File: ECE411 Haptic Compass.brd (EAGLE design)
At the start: 63.5 x 63.2 mm, 40 parts, among them IC1 SN74LVC1G14DBVR, Q1 PBHV8115TLHR, Q2 PBHV8115TLHR, Q3 PBHV8115TLHR, Q4 PBHV8115TLHR, U1 328P, Y1 ECS-160-8-30Q-VY-TR

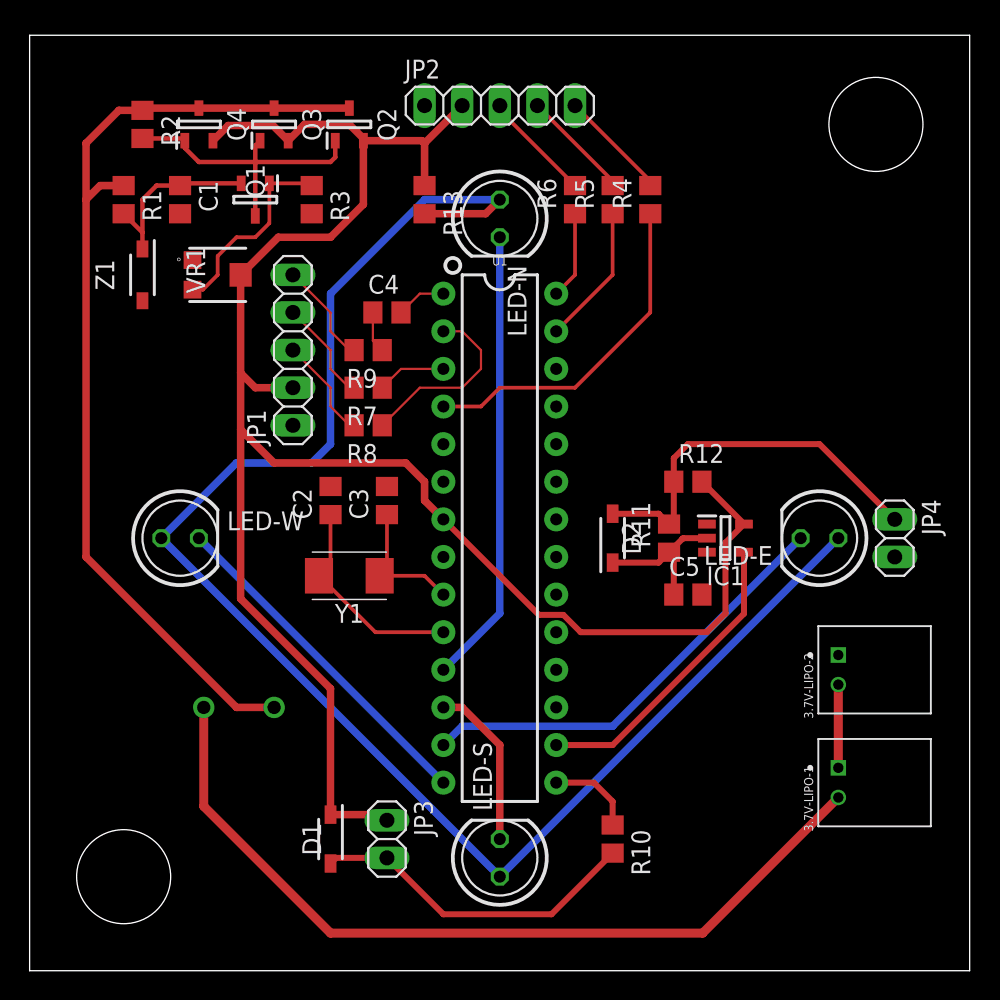
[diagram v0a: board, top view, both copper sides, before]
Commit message: Layout Finish - Ground Plane Added
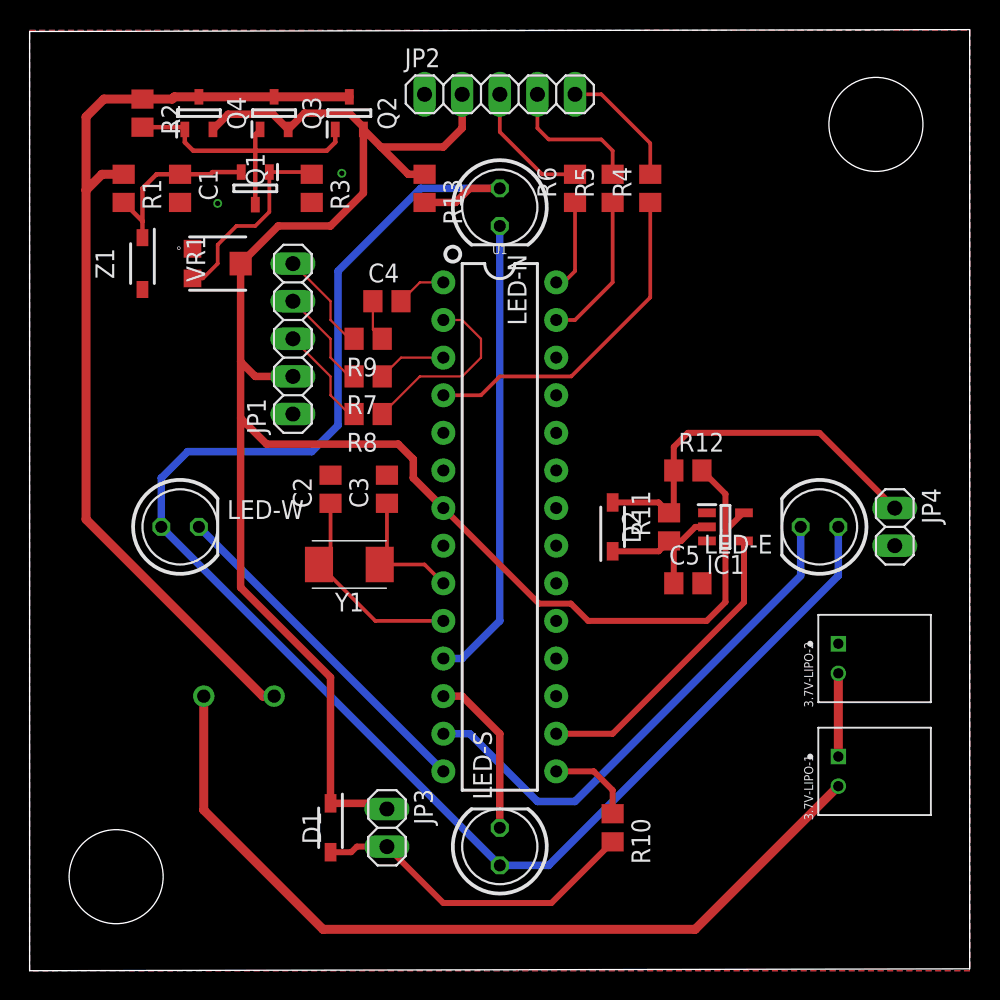
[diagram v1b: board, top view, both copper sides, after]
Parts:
- moved 3.7V-LIPO-1 0.76 mm to (54.6, 13.5)
- moved 3.7V-LIPO-2 0.76 mm to (54.6, 21.1)
- moved C1 0.76 mm to (10.2, 52.8)
- moved C2 0.76 mm to (20.3, 32.5)
- moved C3 0.76 mm to (24.1, 32.5)
- moved C4 0.76 mm to (24.1, 45.2)
- moved C5 0.76 mm to (44.5, 26.2)
- moved D2 0.76 mm to (39.4, 30.0)
- moved IC1 0.76 mm to (47.0, 30.0)
- moved JP1 0.76 mm to (17.8, 42.7)
- moved JP2 0.76 mm to (31.8, 59.2)
- moved JP4 0.76 mm to (58.4, 30.0)
- moved LED-E 0.76 mm to (53.3, 30.0)
- moved LED-N 0.76 mm to (31.8, 51.6)
- moved LED-W 0.76 mm to (10.2, 30.0)
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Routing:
- net LED-EAST: track 29.9 -> 35.6 mm
- net VCC: track 142.3 -> 138.1 mm
- net LED-RAIL: track 108.4 -> 112.4 mm
- net SDA-PORT: track 7.50 -> 9.59 mm
- net SCL-PORT: track 7.50 -> 8.80 mm
- net DRDY-PORT: track 7.50 -> 8.55 mm
- net +V-SUPPLY: track 56.9 -> 57.9 mm
- net SDA: track 9.52 -> 10.3 mm
- net LED-NORTH: track 30.8 -> 31.5 mm
- added copper zone on layer 1, net GND
- added copper zone on layer 16, net GND
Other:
- board size 63.5 x 63.2 mm -> 63.5 x 63.6 mm

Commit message: Placement of switch on top
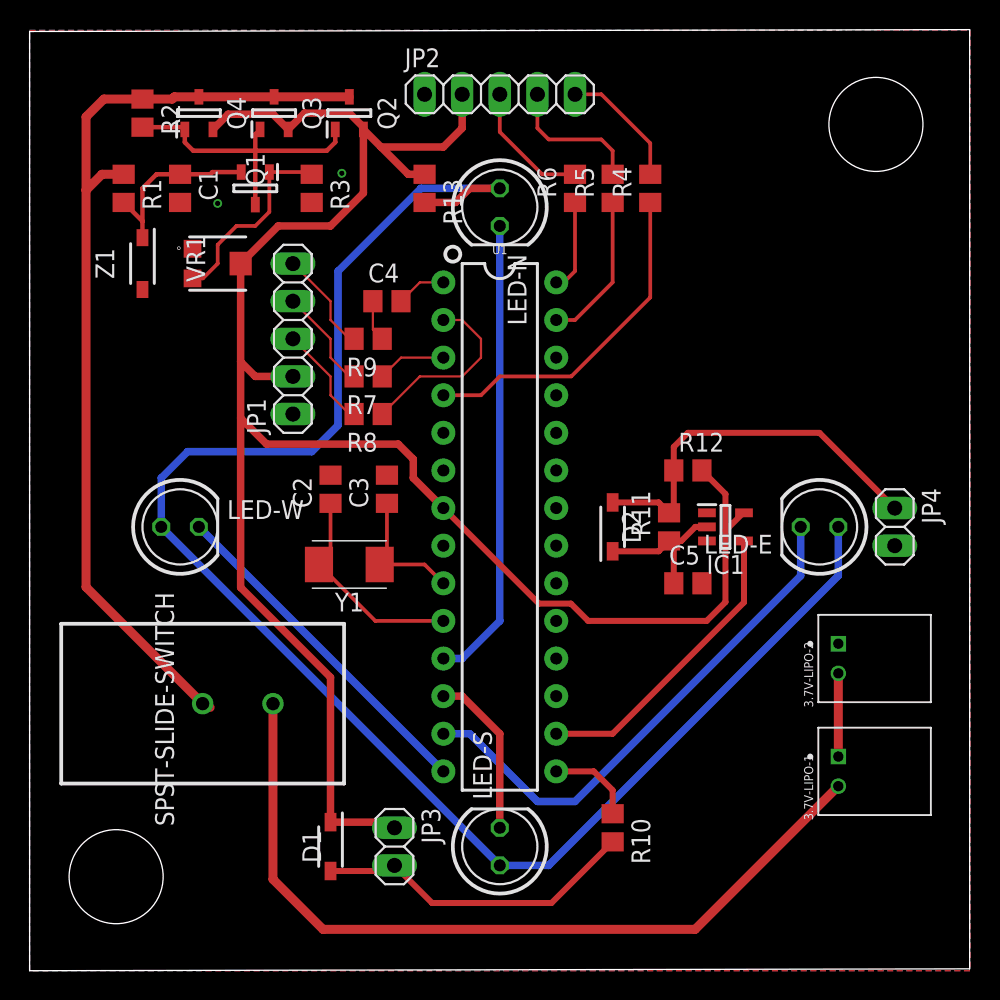
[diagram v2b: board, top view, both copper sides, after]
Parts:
- moved SPST-SLIDE-SWITCH 4.85 mm to (11.7, 18.0), flipped to the top
- moved JP3 1.37 mm to (24.6, 8.38)
- moved D1 1.27 mm to (20.3, 8.38)
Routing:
- net +V-SUPPLY: track 57.9 -> 55.4 mm
- net VCC: track 138.1 -> 139.9 mm
- net BJT-C: track 66.1 -> 64.8 mm
- net JP3-NEG: track 22.5 -> 22.0 mm

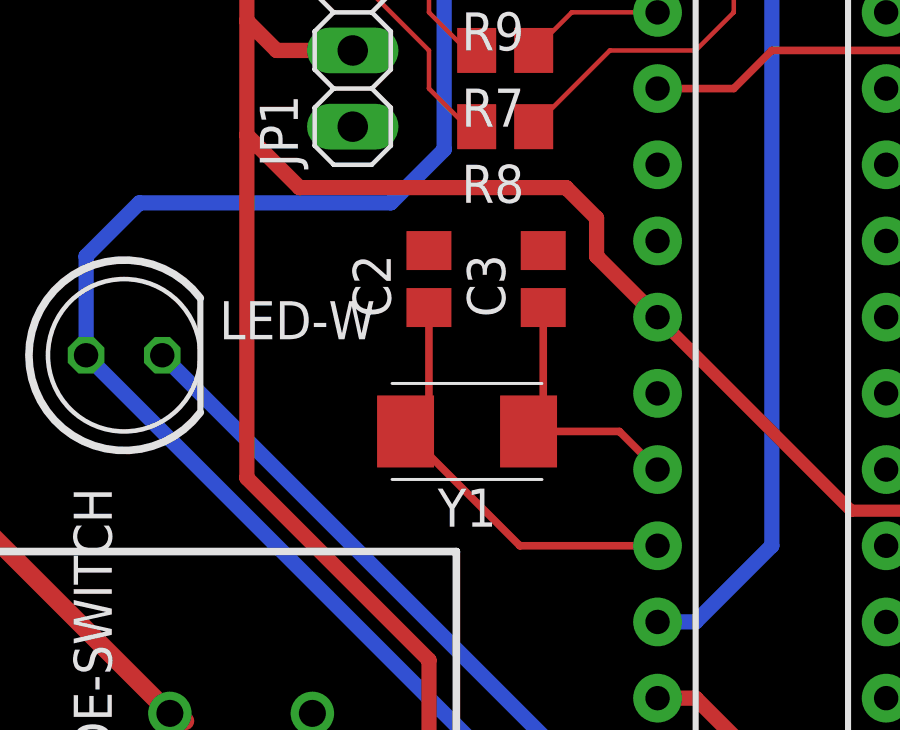
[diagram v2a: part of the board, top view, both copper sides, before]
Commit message: Included 1uF Capacitor next to Vcc for the uPC
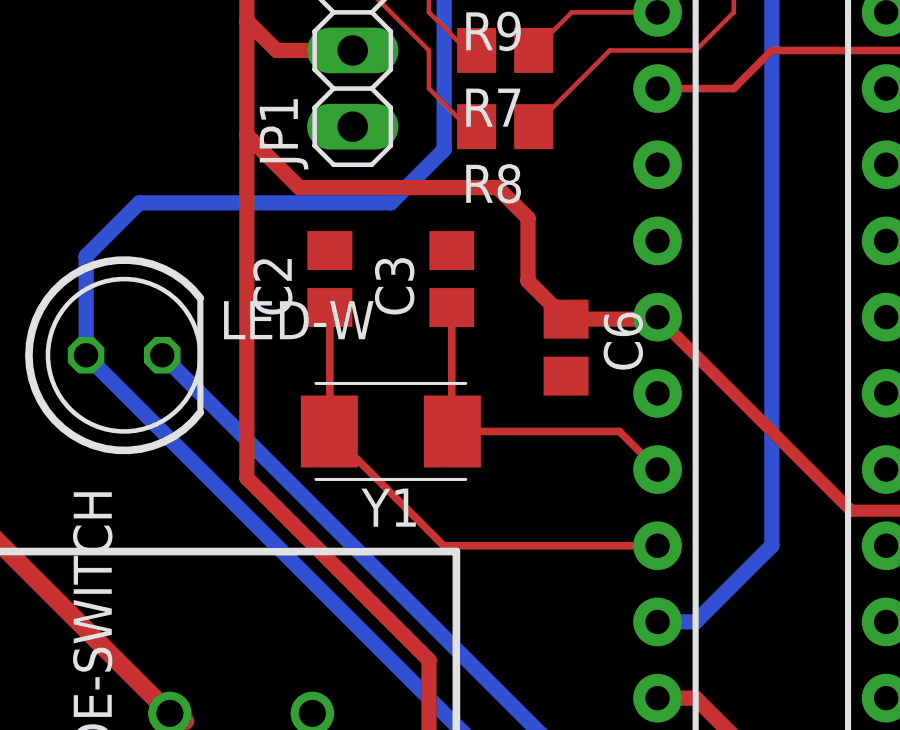
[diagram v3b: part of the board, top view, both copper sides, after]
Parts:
- added C6: 1uF, rcl:C0805
- moved C2 3.30 mm to (17.0, 32.5)
- moved C3 3.05 mm to (21.1, 32.5)
- moved Y1 2.54 mm to (19.1, 27.4)
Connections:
- net GND: now also C6.2
- net VCC: now also C6.1
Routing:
- net N$7: track 9.16 -> 11.5 mm
- net N$5: track 14.4 -> 16.7 mm
- net VCC: track 139.9 -> 140.4 mm
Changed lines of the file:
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@@
 <attribute name="VALUE" x="7.62" y="54.102" size="1.27" layer="27" rot="R270"/>
 </element>
-<element name="C2" library="rcl" library_urn="urn:adsk.eagle:library:334" package="C0805" package3d_urn="urn:adsk.eagle:package:23617/2" value="22pF" x="20.32" y="32.512" smashed="yes" rot="R90">
-<attribute name="NAME" x="19.05" y="31.242" size="1.27" layer="25" rot="R90"/>
-<attribute name="POPULARITY" value="63" x="60.96" y="82.042" size="1.778" layer="27" rot="R90" display="off"/>
-<attribute name="SPICEPREFIX" value="C" x="60.96" y="82.042" size="1.778" layer="27" rot="R90" display="off"/>
-<attribute name="VALUE" x="22.86" y="31.242" size="1.27" layer="27" rot="R90"/>
-</element>
-<element name="C3" library="rcl" library_urn="urn:adsk.eagle:library:334" package="C0805" package3d_urn="urn:adsk.eagle:package:23617/2" value="22pF" x="24.13" y="32.512" smashed="yes" rot="R90">
-<attribute name="NAME" x="22.86" y="31.242" size="1.27" layer="25" rot="R90"/>
-<attribute name="POPULARITY" value="63" x="64.77" y="88.392" size="1.778" layer="27" rot="R90" display="off"/>
-<attribute name="SPICEPREFIX" value="C" x="64.77" y="88.392" size="1.778" layer="27" rot="R90" display="off"/>
-<attribute name="VALUE" x="26.67" y="31.242" size="1.27" layer="27" rot="R90"/>
+<element name="C2" library="rcl" library_urn="urn:adsk.eagle:library:334" package="C0805" package3d_urn="urn:adsk.eagle:package:23617/2" value="22pF" x="17.018" y="32.512" smashed="yes" rot="R90">
+<attribute name="NAME" x="15.748" y="31.242" size="1.27" layer="25" rot="R90"/>
+<attribute name="POPULARITY" value="63" x="57.658" y="82.042" size="1.778" layer="27" rot="R90" display="off"/>
+<attribute name="SPICEPREFIX" value="C" x="57.658" y="82.042" size="1.778" layer="27" rot="R90" display="off"/>
+<attribute name="VALUE" x="19.558" y="31.242" size="1.27" layer="27" rot="R90"/>
+</element>
+<element name="C3" library="rcl" library_urn="urn:adsk.eagle:library:334" package="C0805" package3d_urn="urn:adsk.eagle:package:23617/2" value="22pF" x="21.082" y="32.512" smashed="yes" rot="R90">
+<attribute name="NAME" x="19.812" y="31.242" size="1.27" layer="25" rot="R90"/>
+<attribute name="POPULARITY" value="63" x="61.722" y="88.392" size="1.778" layer="27" rot="R90" display="off"/>
+<attribute name="SPICEPREFIX" value="C" x="61.722" y="88.392" size="1.778" layer="27" rot="R90" display="off"/>
+<attribute name="VALUE" x="23.622" y="31.242" size="1.27" layer="27" rot="R90"/>
 </element>
 <element name="C4" library="rcl" library_urn="urn:adsk.eagle:library:334" package="C0805" package3d_urn="urn:adsk.eagle:package:23617/2" value="100pF" x="24.13" y="45.212" smashed="yes">
@@
 <attribute name="VALUE" x="13.761" y="48.089" size="1.27" layer="27" rot="R270" align="center"/>
 </element>
-<element name="Y1" library="SamacSys_Parts" package="ECS80830QVSTR" value="ECS-160-8-30Q-VY-TR" x="21.59" y="27.432" smashed="yes">
-<attribute name="DESCRIPTION" value="Crystals 16MHz 8pF AEC ESR 50 -40C +150C" x="72.39" y="-25.908" size="1.778" layer="27" display="off"/>
-<attribute name="HEIGHT" value="1.1mm" x="72.39" y="-25.908" size="1.778" layer="27" display="off"/>
-<attribute name="MANUFACTURER_NAME" value="ECS" x="72.39" y="-25.908" size="1.778" layer="27" display="off"/>
-<attribute name="MANUFACTURER_PART_NUMBER" value="ECS-160-8-30Q-VY-TR" x="72.39" y="-25.908" size="1.778" layer="27" display="off"/>
-<attribute name="MOUSER_PART_NUMBER" value="520-160-8-30Q-VYT" x="72.39" y="-25.908" size="1.778" layer="27" display="off"/>
-<attribute name="MOUSER_PRICE-STOCK" value="https://www.mouser.com/Search/Refine.aspx?Keyword=520-160-8-30Q-VYT" x="72.39" y="-25.908" size="1.778" layer="27" display="off"/>
-<attribute name="NAME" x="21.59" y="24.892" size="1.27" layer="25" align="center"/>
-<attribute name="VALUE" x="21.59" y="29.972" size="1.27" layer="27" align="center"/>
+<element name="Y1" library="SamacSys_Parts" package="ECS80830QVSTR" value="ECS-160-8-30Q-VY-TR" x="19.05" y="27.432" smashed="yes">
+<attribute name="DESCRIPTION" value="Crystals 16MHz 8pF AEC ESR 50 -40C +150C" x="69.85" y="-25.908" size="1.778" layer="27" display="off"/>
+<attribute name="HEIGHT" value="1.1mm" x="69.85" y="-25.908" size="1.778" layer="27" display="off"/>
+<attribute name="MANUFACTURER_NAME" value="ECS" x="69.85" y="-25.908" size="1.778" layer="27" display="off"/>
+<attribute name="MANUFACTURER_PART_NUMBER" value="ECS-160-8-30Q-VY-TR" x="69.85" y="-25.908" size="1.778" layer="27" display="off"/>
+<attribute name="MOUSER_PART_NUMBER" value="520-160-8-30Q-VYT" x="69.85" y="-25.908" size="1.778" layer="27" display="off"/>
+<attribute name="MOUSER_PRICE-STOCK" value="https://www.mouser.com/Search/Refine.aspx?Keyword=520-160-8-30Q-VYT" x="69.85" y="-25.908" size="1.778" layer="27" display="off"/>
+<attribute name="NAME" x="19.05" y="24.892" size="1.27" layer="25" align="center"/>
+<attribute name="VALUE" x="19.05" y="29.972" size="1.27" layer="27" align="center"/>
 </element>
 <element name="Z1" library="SamacSys_Parts" package="SOD3716X135N" value="MMSZ4684T1G" x="7.62" y="47.752" smashed="yes" rot="R270">
@@
 <attribute name="NAME" x="5.08" y="47.752" size="1.27" layer="25" rot="R270" align="center"/>
 <attribute name="VALUE" x="8.89" y="47.752" size="1.27" layer="27" rot="R270" align="center"/>
+</element>
+<element name="C6" library="rcl" library_urn="urn:adsk.eagle:library:334" package="C0805" package3d_urn="urn:adsk.eagle:package:23617/2" value="1uF" x="24.892" y="30.226" smashed="yes" rot="R270">
+<attribute name="NAME" x="26.162" y="31.496" size="1.27" layer="25" rot="R270"/>
+<attribute name="POPULARITY" value="63" x="24.892" y="30.226" size="1.778" layer="27" rot="R270" display="off"/>
+<attribute name="SPICEPREFIX" value="C" x="24.892" y="30.226" size="1.778" layer="27" rot="R270" display="off"/>
+<attribute name="VALUE" x="22.352" y="31.496" size="1.27" layer="27" rot="R270"/>
 </element>
 </elements>
@@
 <wire x1="14.25" y1="41.122" x2="15.24" y2="40.132" width="0.508" layer="1"/>
 <wire x1="15.24" y1="40.132" x2="17.78" y2="40.132" width="0.508" layer="1"/>
-<wire x1="24.892" y1="35.56" x2="25.908" y2="34.544" width="0.508" layer="1"/>
-<wire x1="25.908" y1="34.544" x2="25.908" y2="33.274" width="0.508" layer="1"/>
-<wire x1="25.908" y1="33.274" x2="27.94" y2="31.242" width="0.508" layer="1"/>
 <wire x1="14.25" y1="41.122" x2="14.25" y2="37.312" width="0.508" layer="1"/>
 <wire x1="14.25" y1="37.312" x2="16.002" y2="35.56" width="0.508" layer="1"/>
-<wire x1="16.002" y1="35.56" x2="24.892" y2="35.56" width="0.508" layer="1"/>
 <wire x1="14.25" y1="37.312" x2="14.25" y2="25.882" width="0.508" layer="1"/>
 <wire x1="20.32" y1="10.032" x2="24.258" y2="10.032" width="0.508" layer="1"/>
@@
 <wire x1="46.99" y1="29.718" x2="48.194" y2="30.922" width="0.4064" layer="1"/>
 <wire x1="48.194" y1="30.922" x2="48.24" y2="30.922" width="0.4064" layer="1"/>
+<contactref element="C6" pad="1"/>
+<wire x1="16.002" y1="35.56" x2="22.606" y2="35.56" width="0.508" layer="1"/>
+<wire x1="23.622" y1="32.446" x2="24.892" y2="31.176" width="0.508" layer="1"/>
+<wire x1="22.606" y1="35.56" x2="23.622" y2="34.544" width="0.508" layer="1"/>
+<wire x1="23.622" y1="34.544" x2="23.622" y2="32.446" width="0.508" layer="1"/>
+<wire x1="27.94" y1="31.242" x2="27.874" y2="31.176" width="0.508" layer="1"/>
+<wire x1="27.874" y1="31.176" x2="24.892" y2="31.176" width="0.508" layer="1"/>
 </signal>
 <signal name="BATT-SERIES">
@@
 <via x="21.082" y="53.848" extent="1-16" drill="0.35"/>
 <via x="12.7" y="51.816" extent="1-16" drill="0.35"/>
+<contactref element="C6" pad="2"/>
 </signal>
 <signal name="SDA">
@@
 <contactref element="Y1" pad="1"/>
 <contactref element="C2" pad="1"/>
-<wire x1="27.94" y1="23.622" x2="23.35" y2="23.622" width="0.254" layer="1"/>
-<wire x1="23.35" y1="23.622" x2="19.54" y2="27.432" width="0.254" layer="1"/>
-<wire x1="20.32" y1="31.562" x2="20.32" y2="28.212" width="0.254" layer="1"/>
-<wire x1="20.32" y1="28.212" x2="19.54" y2="27.432" width="0.254" layer="1"/>
+<wire x1="27.94" y1="23.622" x2="20.81" y2="23.622" width="0.254" layer="1"/>
+<wire x1="20.81" y1="23.622" x2="17" y2="27.432" width="0.254" layer="1"/>
+<wire x1="17.018" y1="31.562" x2="17.018" y2="27.45" width="0.254" layer="1"/>
+<wire x1="17" y1="27.432" x2="17.018" y2="27.45" width="0.254" layer="1"/>
 </signal>
 <signal name="N$7">
@@
 <contactref element="Y1" pad="2"/>
 <contactref element="C3" pad="1"/>
-<wire x1="24.13" y1="31.562" x2="24.13" y2="27.922" width="0.254" layer="1"/>
-<wire x1="24.13" y1="27.922" x2="23.64" y2="27.432" width="0.254" layer="1"/>
-<wire x1="23.64" y1="27.432" x2="26.67" y2="27.432" width="0.254" layer="1"/>
+<wire x1="21.082" y1="31.562" x2="21.082" y2="27.45" width="0.254" layer="1"/>
+<wire x1="21.1" y1="27.432" x2="21.082" y2="27.45" width="0.254" layer="1"/>
+<wire x1="21.1" y1="27.432" x2="26.67" y2="27.432" width="0.254" layer="1"/>
 <wire x1="26.67" y1="27.432" x2="27.94" y2="26.162" width="0.254" layer="1"/>
 </signal>
